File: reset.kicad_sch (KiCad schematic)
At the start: 13 parts, among them Q1 BSS138, Q2 BSS138

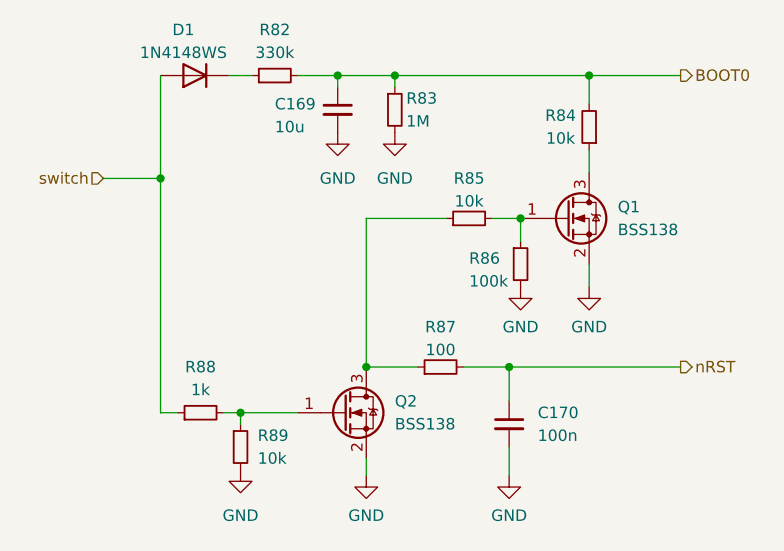
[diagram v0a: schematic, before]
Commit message: Routed a lot of the pcb, additionally fixed issues with wrong layout
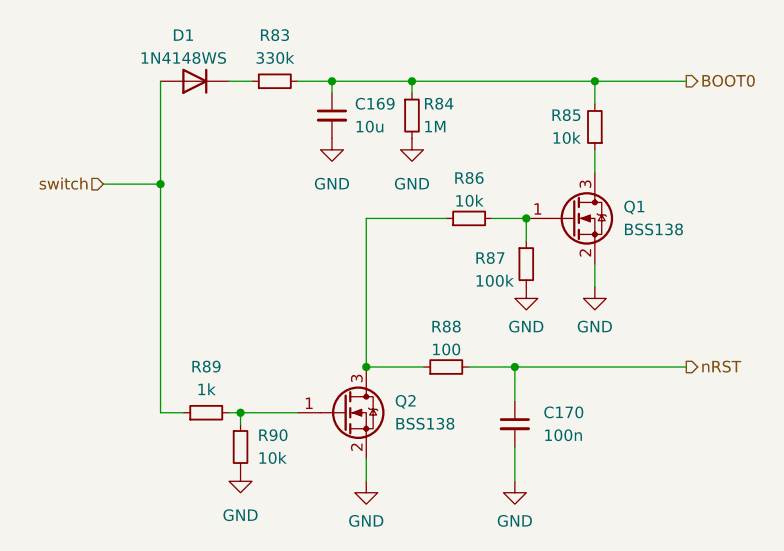
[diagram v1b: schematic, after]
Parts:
- C169: footprint Capacitor_SMD:C_1206_3216Metric -> Capacitor_SMD:C_0402_1005Metric
- renumbered R82 to R83, R83 to R84, R84 to R85, R85 to R86, R86 to R87, R87 to R88, R88 to R89, R89 to R90
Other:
- moved on the sheet: C170, D1, Q1, R83, R84, R85, R87, R88, R89
